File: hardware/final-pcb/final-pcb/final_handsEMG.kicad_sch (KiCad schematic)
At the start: 91 parts, among them J1 Conn_02x13_Odd_Even, J2 Conn_01x02, U1 ADS1299CPAG, U2 STM32L496ZGT6, U3 LM2664M6/NOPB, U4 TLV70025QDDCRQ1, U5 MCP1754T-3302E/OT, U6 TPS72325DBVR

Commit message: added ltc3586 and ads1299 LDOs (3.31.25)
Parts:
- removed C29, C31, C33, C37: 10uF, GRM188C80G106KE47D:CAPC1608X90N, symbol Device:C_Small
- removed C30: 0.01uF, CC0402KRX7R7BB103:CC0402N_YAG, symbol Device:C_Small
- removed C32, C35, C36, C38, C40: 2.2uF, GRM155C80J225ME95D:CAPC1005X55N, symbol Device:C_Small
- removed C39: 2.2uF, GRM155R61C225KE44D:CAP_GRM155R61C225KE44D_MUR, symbol Device:C_Small
- removed D9: D_Small, symbol Device:D_Small
- removed J2: Conn_01x02, symbol Connector_Generic:Conn_01x02
- removed U3: LM2664M6/NOPB, symbol LM2664M6/NOPB:LM2664M6_NOPB
- removed U4: TLV70025QDDCRQ1, TLV70025QDDCRQ1:SOT95P280X110-5N, symbol TLV70025QDDCRQ1:TLV70025QDDCRQ1
- removed U5: MCP1754T-3302E/OT, symbol MCP1754T-3302E/OT:MCP1754T-3302E_OT
- removed U6: TPS72325DBVR, TPS72325DBVR:SOT95P280X145-5N, symbol TPS72325DBVR:TPS72325DBVR
- removed sC42: 4.7uF, TAJA475K016R:CAPMP3216X166, symbol Device:C_Polarized_Small
- removed sLD7: Red, LED-SMD-RED-DIFFUSED_0603_:LED-0603, symbol Device:D_Small
- removed sLD8: Green, SMD-LED-CLEAR-GREEN_0603_:LED-0603, symbol Device:D_Small
- removed sR41: 330, symbol Device:R_Small
- removed sR45: 620, symbol Device:R_Small
- removed sR48: 22K, symbol Device:R_Small
- removed sR49, sR51: 47K, symbol Device:R_Small
- removed sR52: 10K, RC0603FR-0710KL:RESC1607X60N, symbol Device:R_Small
- removed sT2: 9013, symbol Transistor_BJT:Q_NPN_BEC
- removed sU12: STMPS2151STR, symbol STMPS2151STR:STMPS2151STR
- added C45, C46, C49, C51, C60, C61, C65, C66, pC2, pC21, pC23, pC3: 10uF, symbol Device:C_Small
- added C47, C48, C50, C58, C62, pC1, pC11, pC4, pC5, pC8, pC9: 1uF, symbol Device:C_Small
- added C57, pC16, pC26, pC27, pC28, pC29: 0.1uF, symbol Device:C_Small
- added C59, C63, C64, pC10: 2.2uF, symbol Device:C_Small
- added C67: 0.01uF, symbol Device:C_Small
- added L1, L2, L4, L5, pL1: 3.3uH, symbol Device:L_Small
- added R17: 2K, symbol Device:R_Small
- added U6: TPS60403DBVT, DBV5, symbol TPS60403DBVT:TPS60403DBVT
- added U8: TPS72325DBVT, TPS72325DBVT:SOT95P280X145-5N, symbol TPS72325DBVT:TPS72325DBVT
- added U9: TPS73225DBVT, DBV5_TEX, symbol TPS73225DBVT:TPS73225DBVT
- added dD4: RED, symbol Device:LED_Small
- added dD5: GREEN, symbol Device:LED_Small
- added dR3: 330, symbol Device:R_Small
- added dR4: 990, symbol Device:R_Small
- added dR6, dR7, pR32, pR33, pR34, pR35, pR5, pR7: 1K, symbol Device:R_Small
- added dU1: FT231XQ-R, symbol FT231XQ-R:FT231XQ-R
- added pC12, pC13: 100uF, symbol Device:C_Small
- added pC14: 47uF, symbol Device:C_Small
- added pC15, pC20, pC22, pC24: 10pF, symbol Device:C_Small
- added pC17: 330pF, symbol Device:C_Small
- added pC18: 33pF, symbol Device:C_Small
- added pC19, pC6, pC7: 22uF, symbol Device:C_Small
- added pD2: GREEN (CHRG), symbol Device:D_Small
- added pD3: RED (FAULT), symbol Device:D_Small
- added pJP2, pJP3, pJP4, pJP5, pJP6, pJP7, pJP8: TMM-103-02-L-S, CONN_TMM-103-XX-XX-S_SAI, symbol TMM-103-02-L-S:TMM-103-02-L-S
- added pL2, pL3: 2.2uH, symbol Device:L_Small
- added pL4, pL5: 4.7uH, symbol Device:L_Small
- added pQ1: PMOS, symbol Simulation_SPICE:PMOS
- added pR10, pR12, pR4: 0, symbol Device:R_Small
- added pR13, pR18, pR23, pR26: 20, symbol Device:R_Small
- added pR14: 88.7k, symbol Device:R_Small
- added pR15: 16.9K, symbol Device:R_Small
- added pR16: 3.01K, symbol Device:R_Small
- added pR19: 15K, symbol Device:R_Small
- added pR2, pR29, pR30, pR31: 1, symbol Device:R_Small
- added pR20: 324K, symbol Device:R_Small
- added pR21: 121K, symbol Device:R_Small
- added pR22: 105K, symbol Device:R_Small
- added pR24: 806K, symbol Device:R_Small
- added pR25: 649K, symbol Device:R_Small
- added pR27: 232K, symbol Device:R_Small
- added pR28: 464K, symbol Device:R_Small
- added pR3, pR9: 100K, symbol Device:R_Small
- added pR6, pR8: 2.2K, symbol Device:R_Small
- added pU1: LTC3586EUFE-3-PBF, symbol LTC3586EUFE-3#PBF:LTC3586EUFE-3-PBF
- added sJ2: S2B-PH-K-SLFSN, symbol S2B_PH_K_S_LF__SN:S2B-PH-K-SLFSN
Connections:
- net +2V5: now also C57.1, C61.1, L5.2
- net +3V3: now also pC19.1, pR18.1, pU1.16 (VOUT3), pU1.17 (VOUT3); no longer C12.1, C14.1, U1.48 (DVDD), U1.50 (DVDD), U2.106 (VDDUSB), U2.108 (VDD__6), U2.121 (VDD__7), U2.131 (VDDIO2__1), U2.144 (VDD__8), U2.17 (VDD), U2.39 (VDD__1), U2.52 (VDD__2), U2.62 (VDD__3), U2.72 (VDD__4), U2.84 (VDD__5), U2.95 (VDDIO2), sC28.1, sC29.1, sC30.1, sC31.1, sC32.1, sC33.1, sC34.1, sC49.1, sC50.1, sC51.1, sC52.1, sC53.1, sC54.1, sC60.1, sC61.1, sJ3.3, sL3.1
- net -2V5: now also C57.2, C66.1, L4.2
- net GND: now also R17.2, dU1.13 (GND), dU1.21 (GND), dU1.3 (GND), pC1.2, pC10.2, pC11.2, pC12.2, pC14.2, pC16.2, pC19.2, pC21.1, pC23.1, pC26.2, pC27.2, pC28.2, pC29.2, pC3.2, pC4.2, pC5.2, pC6.2, pC7.2, pC8.2, pC9.2, pJP2.3, pJP3.3, pJP4.3, pJP5.3, pJP6.3, pJP7.3, pJP8.3, pR15.1, pR16.2, pR2.2, pR22.2, pR25.2, pR28.2, pR29.1, pR30.1, pR31.1, pR9.1, pU1.39 (EPAD), sJ2.2
- net GNDA: now also C45.2, C46.2, C47.2, C49.2, C50.2, C51.2, C58.2, C59.2, C60.2, C61.2, C62.2, C63.2, C64.2, C65.2, C66.2, C67.2, U6.4 (GND), U8.1 (GND), U9.2 (GND)
- net PA11: now also dU1.9 (USBDM)
- net PA12: now also dU1.8 (USBDP)
- net USB_VBUS renamed AVBUS
- net AVBUS: now also dU1.12 (VCC), pC2.1, pC3.1, pC8.1, pJP2.1, pJP3.1, pR3.1, pU1.35 (VBUS), pU1.36 (VBUS)
- new net: C59.1, C60.1, L5.1, U9.5 (OUT)
- new net: dD4.1 (K), dR3.1
- new net: pJP6.1, pR33.1
- new net: C48.1, U6.5 (CFLY+)
- new net: C48.2, U6.3 (CFLY-)
- new net: dR6.1, dU1.1 (RXD)
- new net: dR4.1, dU1.14 (CBUS1)
- new net: dR7.2, dU1.17 (TXD)
- new net: dR3.2, dU1.7 (CBUS2)
- new net: pC18.1, pR18.2, pR20.1
- new net: pC15.1, pR13.1, pR14.2
- new net: pJP5.1, pR32.1
- new net: C64.1, C65.1, L4.1, U8.5 (OUT)
- new net: C67.1, U8.4 (NR)
- new net: pC24.2, pR26.2, pR27.1
- new net: pC17.2, pR19.1
- new net: pD2.1 (K), pR5.1
- new net: pR10.1, pR9.2
- new net: pJP8.1, pR35.1
- new net: dD5.1 (K), dR4.2
- new net: pC22.2, pR23.2, pR24.1
- new net: pD3.1 (K), pR7.1
- new net: pC18.2, pR21.1
- new net: pC2.2, pR2.1
- new net: pC13.2, pR29.2, pR30.2, pR31.2
- new net: C62.1, U9.4 (NR/FB)
- new net: pJP7.1, pR34.1
- new net *CHRG: pR5.2, pR6.2, pU1.30 (*CHRG)
- new net *FAULT: pR7.2, pR8.2, pU1.38 (*FAULT)
- new net +5V: C45.1, L1.1, pC14.1, pR13.2, pU1.6 (VOUT4), pU1.7 (VOUT4)
- new net -5V: C51.1, L2.1
- new net -5VCC: C49.1, C50.1, L2.2, U6.1 (OUT)
- new net 3V3OUT: dU1.10 (3V3OUT)
- new net 5VCC: C46.1, C47.1, C58.1, C63.1, L1.2, U6.2 (IN), U8.2 (IN), U8.3 (EN), U9.1 (IN), U9.3 (EN)
- new net AVIN3: pC11.1, pR4.1, pU1.14 (VIN3)
- new net BAT: pC13.1, pQ1.1 (D), pU1.32 (BAT), sJ2.1
- new net CLPROG: pC16.1, pR16.1, pU1.4 (CLPROG)
- new net DTR: dU1.18 (DTR#)
- new net DVDD: C12.1, C14.1, U1.48 (DVDD), U1.50 (DVDD), U2.106 (VDDUSB), U2.108 (VDD__6), U2.121 (VDD__7), U2.131 (VDDIO2__1), U2.144 (VDD__8), U2.17 (VDD), U2.39 (VDD__1), U2.52 (VDD__2), U2.62 (VDD__3), U2.72 (VDD__4), U2.84 (VDD__5), U2.95 (VDDIO2), dD4.2 (A), dD5.2 (A), dU1.11 (RESET#), dU1.20 (VCCIO), sC28.1, sC29.1, sC30.1, sC31.1, sC32.1, sC33.1, sC34.1, sC49.1, sC50.1, sC51.1, sC52.1, sC53.1, sC54.1, sC60.1, sC61.1, sJ3.3, sL3.1
- new net EN1: pC26.1, pJP5.2, pU1.21 (EN1)
- new net EN2: pC27.1, pJP6.2, pU1.20 (EN2)
- new net EN3: pC28.1, pJP7.2, pU1.18 (EN3)
- new net EN4: pC29.1, pJP8.2, pU1.33 (EN4)
- new net FB1: pC24.1, pR27.2, pR28.1, pU1.28 (FB1)
- new net FB2: pC22.1, pR24.2, pR25.1, pU1.23 (FB2)
- new net FB3: pC20.2, pR19.2, pR20.2, pR21.2, pR22.1, pU1.11 (FB3)
- new net FB4: pC15.2, pR14.1, pR15.2, pU1.10 (FB4)
- new net FTD_RX: dR6.2
- new net FTD_TX: dR7.1
- new net GATE: pQ1.2 (G), pU1.31 (GATE)
- new net ILIM0: pJP2.2, pU1.1 (ILIM0)
- new net ILIM1: pJP3.2, pU1.2 (ILIM1)
- new net LDO3V3: pC1.1, pD2.2 (A), pD3.2 (A), pR12.2, pR32.2, pR33.2, pR34.2, pR35.2, pR6.1, pR8.1, pU1.3 (LDO3V3)
- new net LDOO3V3: pJP4.1
- new net MODE: pJP4.2, pU1.9 (MODE)
- new net NTC: pR10.2, pR3.2, pU1.5 (NTC)
- new net PROG: R17.1, pU1.29 (PROG)
- new net PVIN3: pC10.1, pC12.1, pC4.1, pC5.1, pC6.1, pC7.1, pC9.1, pL1.2, pL2.2, pQ1.3 (S), pR12.1, pR4.2, pU1.15 (VIN3), pU1.22 (VIN4), pU1.24 (VIN2), pU1.27 (VIN1), pU1.34 (VOUT)
- new net SW: pL1.1, pU1.37 (SW)
- new net SW1: pL5.1, pU1.26 (SW1)
- new net SW2: pL4.1, pU1.25 (SW2)
- new net SW4: pL2.1, pU1.8 (SW4)
- new net SWAB3: pL3.2, pU1.13 (SWAB3)
- new net SWCD3: pL3.1, pU1.19 (SWCD3)
- new net VC3: pC17.1, pC20.1, pU1.12 (VC3)
- new net VOUT1: pC23.2, pL5.2, pR26.1
- new net VOUT2: pC21.2, pL4.2, pR23.1
- no-connect marks 98 -> 104
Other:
- moved on the sheet: sD10, sJ3, sU13

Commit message: final pcb update 4.2.25 (added dongle usb stuff)
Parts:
- removed dD4: RED, symbol Device:LED_Small
- removed dD5: GREEN, symbol Device:LED_Small
- removed dU1: FT231XQ-R, symbol FT231XQ-R:FT231XQ-R
- added L3: L_Small, symbol Device:L_Small
- added U3: FT231XQ-R, FT231XQ-R:QFN20_FT231XQ_FTD, symbol FT231XQ-R:FT231XQ-R
- added dC1: 0.01uF, CC0402KRX7R7BB103:CC0402N_YAG, symbol Device:C_Small
- added dC2, dC3: 47pF, GRM0335C1E470JA01D:G-033_MUR, symbol Device:C_Small
- added dD3: D_Small, ESDALC6V1-1M2:SOD882_STM, symbol Device:D_Small
- added dD4: RED, LTST-C191KRKT:LED_LTST-C191KRKT_LTO, symbol Device:D_Small
- added dD5: GREEN, LTST-C191KGKT:LED_LTST-C191KGKT_LTO, symbol Device:D_Small
- added dF1: Fuse_Small, MF-MSMF050-2:FUSE_F050-2, symbol Device:Fuse_Small
- added dR1, dR2: 27, RC0402FR-0722RL:RC0402N_YAG, symbol Device:R_Small
- added sC42: 4.7uF, symbol Device:C_Polarized_Small
- added sLD7: Red, LED-SMD-RED-DIFFUSED_0603_:LED-0603, symbol Device:D_Small
- added sLD8: Green, SMD-LED-CLEAR-GREEN_0603_:LED-0603, symbol Device:D_Small
- added sR41: 330, RC0603FR-07330RL:RESC1607X60N, symbol Device:R_Small
- added sR45: 620, RC0603FR-07620RL:RESC1608X55N, symbol Device:R_Small
- added sR48: 22K, RC0603FR-0722KL:RESC1607X60N, symbol Device:R_Small
- added sR49, sR51: 47K, RC0603FR-0747KL:RESC1608X55, symbol Device:R_Small
- added sR52: 10K, RC0603FR-0710KL:RESC1607X60N, symbol Device:R_Small
- added sT2: 9013, MMBT9013:SOT-23, symbol Transistor_BJT:Q_NPN_BEC
- added sU12: STMPS2151STR, STMPS2151STR:SOT95P280X145-5N, symbol STMPS2151STR:STMPS2151STR
- C45, C46, C51, C60, C61, C65, C66: footprint (none) -> GRM219R61A106KE44D:CAPC2012X95N
- C47, C48, C58, C62: footprint (none) -> GRM188R61E105KA12D:CAPC1608X90N
- C49: renamed from C50; footprint (none) -> GRM188R61E105KA12D:CAPC1608X90N
- C50: renamed from C49; footprint (none) -> GRM219R61A106KE44D:CAPC2012X95N
- C57: footprint (none) -> GRM188R71H104KA93D:CAPC1608X90N
- C59, C63, C64: footprint (none) -> GRM185R60J225KE26D:CAP_GRM18_MUR
- C67: footprint (none) -> GRM188R71H103KA01D:CAPC1608X90N
- U6: footprint DBV5 -> (none)
- U9: footprint DBV5_TEX -> (none)
- dR3: footprint (none) -> RC0402JR-07330RL:RC0402N_YAG
- dR4: value 990 -> 330; footprint (none) -> RC0402JR-07330RL:RC0402N_YAG
- dR6, dR7: footprint (none) -> RT0402FRE071KL:RC0402N_YAG
- pJP2, pJP3, pJP4, pJP5, pJP6, pJP7, pJP8: footprint CONN_TMM-103-XX-XX-S_SAI -> (none)
- renumbered R17 to pR17
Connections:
- net DVDD is gone; now on net +3V3: C12.1, C14.1, U1.48 (DVDD), U1.50 (DVDD), U2.106 (VDDUSB), U2.108 (VDD__6), U2.121 (VDD__7), U2.131 (VDDIO2__1), U2.144 (VDD__8), U2.17 (VDD), U2.39 (VDD__1), U2.52 (VDD__2), U2.62 (VDD__3), U2.72 (VDD__4), U2.84 (VDD__5), U2.95 (VDDIO2), sC28.1, sC29.1, sC30.1, sC31.1, sC32.1, sC33.1, sC34.1, sC49.1, sC50.1, sC51.1, sC52.1, sC53.1, sC54.1, sC60.1, sC61.1, sJ3.3, sL3.1
- net +3V3: now also sR41.2, sR45.2, sR51.2, sU12.5 (IN)
- net 3V3OUT: now also U3.10 (3V3OUT), U3.11 (RESET#), U3.20 (VCCIO), dD4.2 (A), dD5.2 (A)
- net AVBUS: now also U3.12 (VCC), dD3.1 (K), dF1.2, sC42.1, sR49.2, sU12.1 (OUT); no longer pJP2.1, pJP3.1, sCN14.1 (VBUS), sR54.2
- net GND: now also U3.13 (GND), U3.21 (GND), U3.3 (GND), dC1.2, dC2.2, dC3.2, dD3.2 (A), sC42.2, sR48.1, sR52.2, sT2.2 (E), sU12.2 (GND)
- net PA11: no longer sCN14.2 (D-), sU13.1 (I/O1), sU13.6 (I/O1)
- net PA12: no longer sCN14.3 (D+), sU13.3 (I/O2), sU13.4 (I/O2)
- net CBUS2: now reaches dR3.1
- net CBUS2: now also U3.7 (CBUS2)
- net RXD: now reaches dR6.1
- net at dR4.1: now also dD5.1 (K)
- net at dR7.2: now also U3.17 (TXD)
- net at dR3.2: now also dD4.1 (K)
- net CBUS1: now reaches dR4.2
- net CBUS1: now also U3.14 (CBUS1)
- net FTD_RX: no longer names the net of dR6.2
- net FTD_RX: now also U3.1 (RXD)
- net FTD_TX renamed TXD
- new net: dC3.1, dR1.1, sCN14.3 (D+)
- new net: sLD7.1 (K), sR51.1, sU12.3 (FAULT)
- new net: sLD7.2 (A), sR45.1
- new net: sLD8.1 (K), sT2.3 (C)
- new net: sLD8.2 (A), sR41.1
- new net: dC2.1, dR2.1, sCN14.2 (D-)
- new net: L3.1, dC1.1, sCN14.1 (VBUS)
- new net: sR48.2, sR49.1, sT2.1 (B)
- new net: sR52.1, sU12.4 (EN)
- new net: L3.2, dF1.1
- new net DTR#: U3.18 (DTR#)
- new net USB_DN: U3.9 (USBDM), dR2.2, sU13.1 (I/O1), sU13.6 (I/O1)
- new net USB_DP: U3.8 (USBDP), dR1.2, sU13.3 (I/O2), sU13.4 (I/O2)
- new net USB_VBUS: pJP2.1, pJP3.1, sR54.2
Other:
- moved on the sheet: sU13

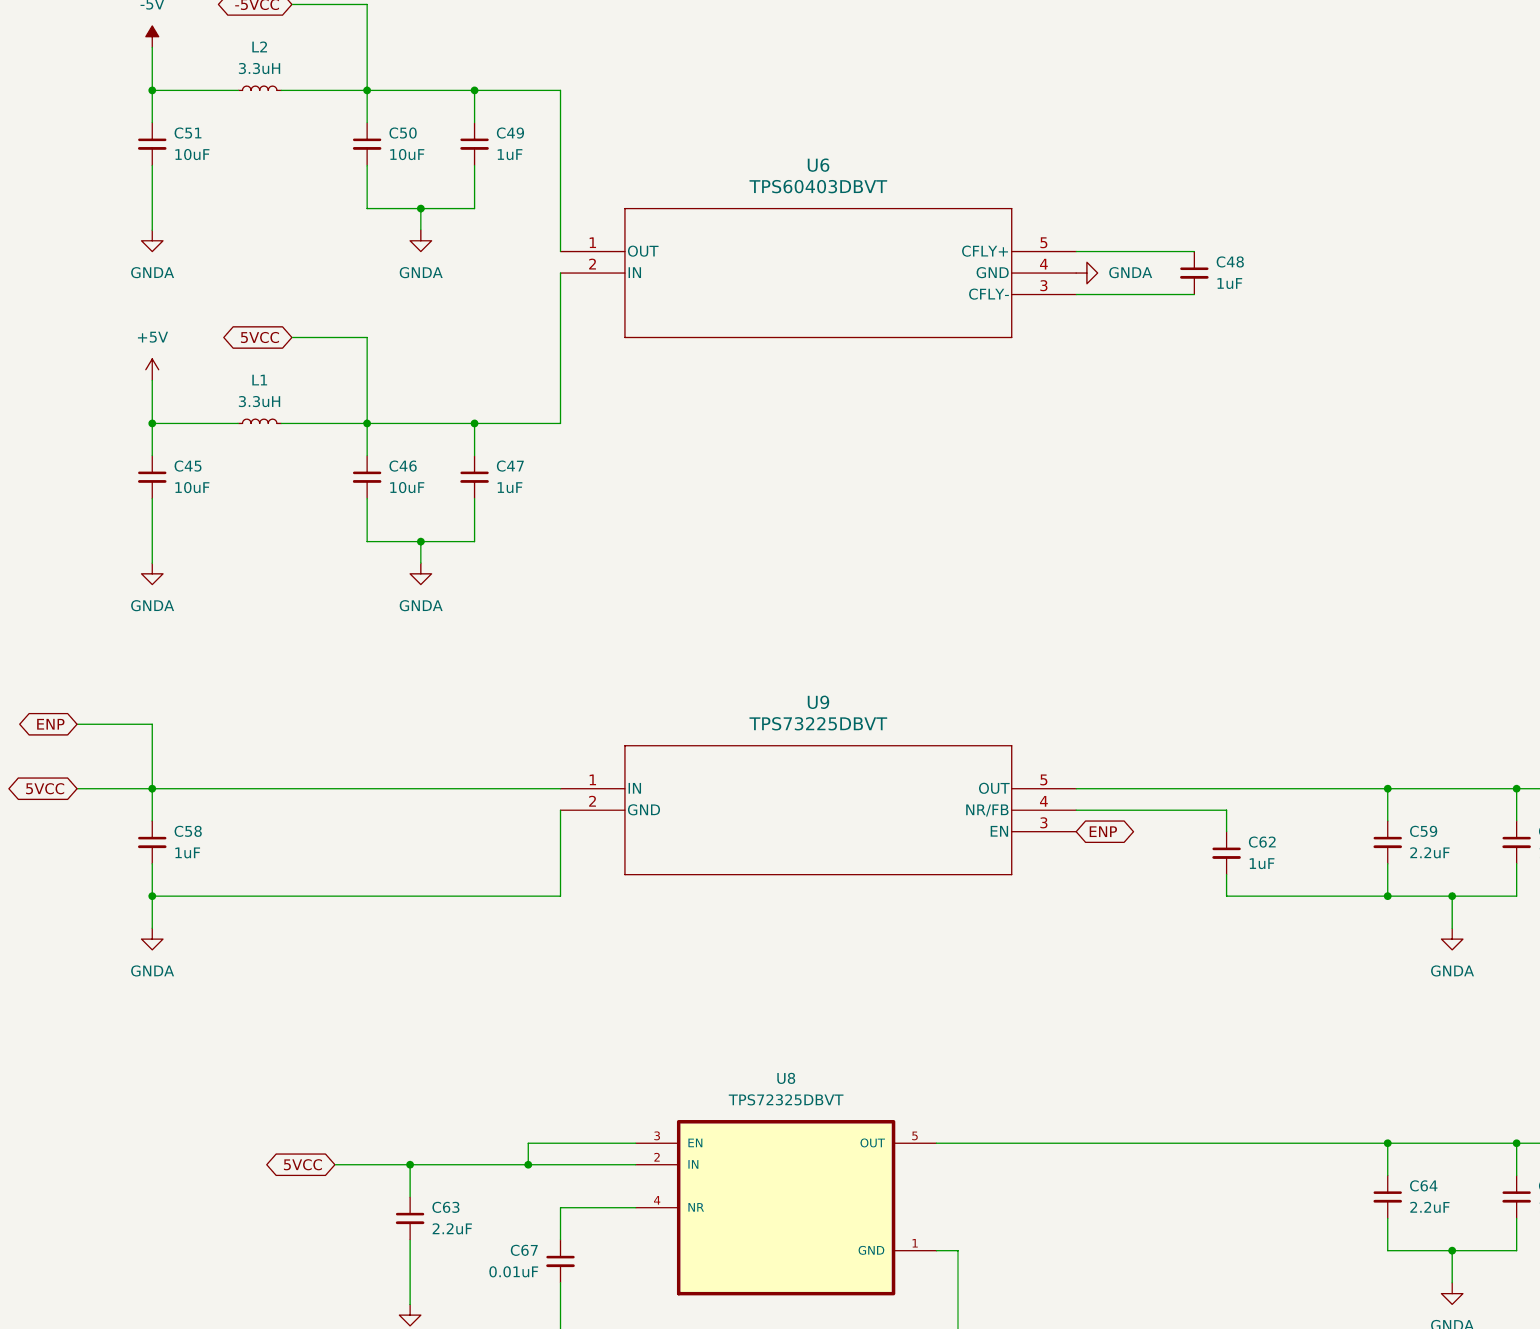
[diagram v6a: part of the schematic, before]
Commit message: Added ECG portions to the final, corrected -5 points
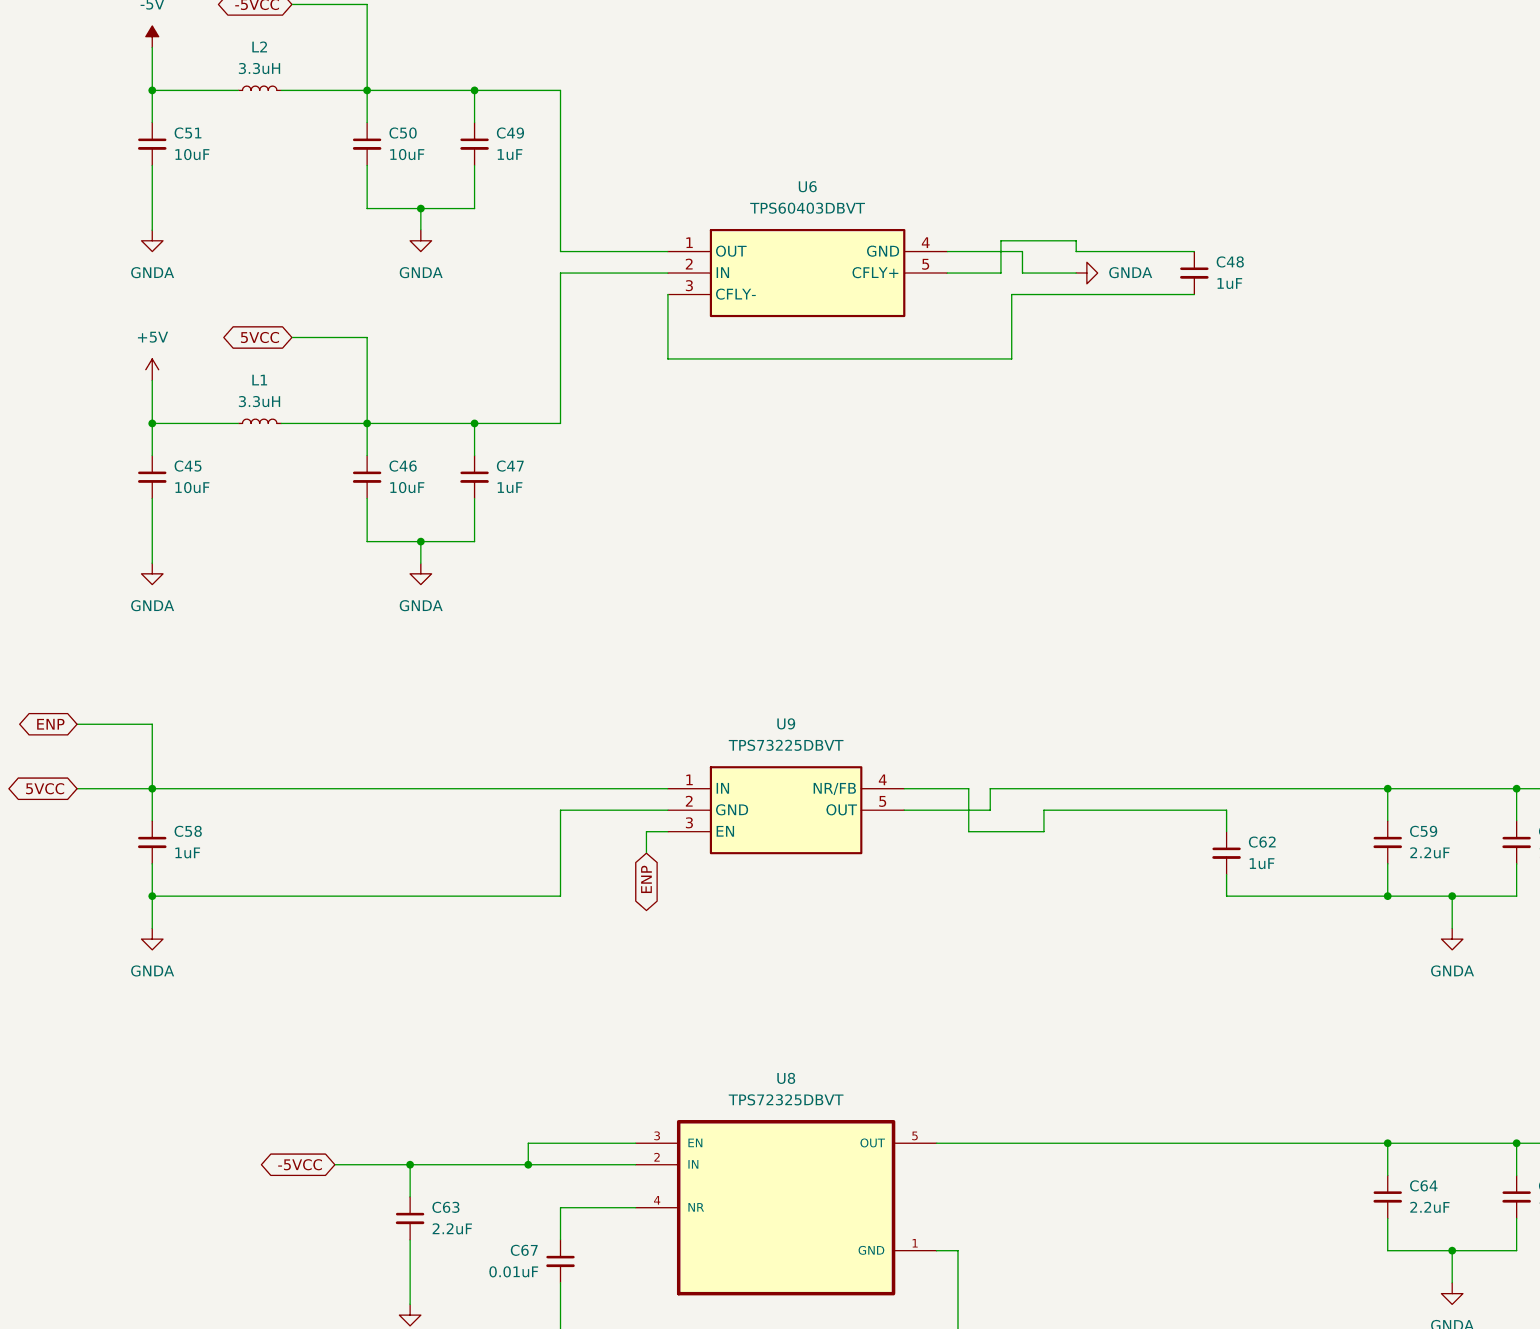
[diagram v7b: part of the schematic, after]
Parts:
- U6: footprint (none) -> SOT95P280X145-5N; Arrow Part Number (none) -> TPS60403DBVT; Arrow Price/Stock (none) -> https://www.arrow.com/en/products/tps60403dbvt/texas-instru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; Height (none) -> 1.45; Manufacturer_Name (none) -> Texas Instruments; Manufacturer_Part_Number (none) -> TPS60403DBVT; Mouser Part Number (none) -> 595-TPS60403DBVT; Mouser Price/Stock (none) -> https://www.mouser.co.uk/ProductDetail/Texas-Instruments/TP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
- U9: footprint (none) -> SOT95P280X145-5N; Arrow Part Number (none) -> TPS73225DBVT; Arrow Price/Stock (none) -> https://www.arrow.com/en/products/tps73225dbvt/texas-instru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; Height (none) -> 1.45; Manufacturer_Name (none) -> Texas Instruments; Manufacturer_Part_Number (none) -> TPS73225DBVT; Mouser Part Number (none) -> 595-TPS73225DBVT; Mouser Price/Stock (none) -> https://www.mouser.co.uk/ProductDetail/Texas-Instruments/TP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
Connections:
- net -5VCC: now also C63.1, U8.2 (IN), U8.3 (EN)
- net 5VCC: no longer C63.1, U8.2 (IN), U8.3 (EN)
